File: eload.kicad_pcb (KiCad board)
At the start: 2 copper layers, 78.7 x 99.1 mm, 34 parts, among them J1 Device Power, J2 Input, J3 Conn_01x16_Socket, J4 SWD Header, J5 Conn_01x14_Pin, Q1 TIP122, U1 LM1117DT-3.3, U2 STM32F103C8T6, U3 AD8629, U4 MCP4725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

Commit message: WIP
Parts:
- added F1: 1.5A, Resistor_THT:R_Axial_DIN0204_L3.6mm_D1.6mm_P7.62mm_Horizontal, F.Cu at (50.3, 64.9)
- J3: value Conn_01x16_Socket -> JST Header
- J5: value Conn_01x14_Pin -> ~
- U3: footprint Package_SO:SOP-8_3.76x4.96mm_P1.27mm -> Package_SO:JEITA_SOIC-8_3.9x4.9mm_P1.27mm
- moved TP7 136.6 mm to (40.0, 56.0)
- moved TP3 102.4 mm to (32.0, 79.2)
- moved TP4 101.0 mm to (37.3, 75.9)
- moved TP1 87.6 mm to (39.2, 91.5)
- moved TP2 86.0 mm to (42.5, 91.5)
- moved TP6 82.2 mm to (80.9, 60.2)
- moved TP5 73.1 mm to (82.2, 67.0)
- moved Y1 50.9 mm to (49.2, 85.5), turned to 180 degrees
- moved J4 50.1 mm to (20.8, 132.9), turned to 180 degrees
- moved C8 49.4 mm to (75.6, 75.4), turned to 180 degrees
- moved C3 45.2 mm to (51.8, 93.5), turned to 180 degrees
- moved R4 44.6 mm to (81.2, 70.2), turned to 180 degrees
- moved R2 43.6 mm to (69.5, 86.5)
- moved U2 43.6 mm to (59.3, 86.5)
- moved R1 43.6 mm to (68.5, 89.0)
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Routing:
- net VCC: track 0.00 -> 26.3 mm
- net /VCC_sense: track 0.00 -> 25.8 mm
- net +3.3V: track 0.00 -> 12.2 mm
- net /Vctrl: track 0.00 -> 11.4 mm
- net Net-(Q1-B): track 0.00 -> 10.8 mm
- net /Vin: track 0.00 -> 8.61 mm
- net +5V: track 0.00 -> 8.39 mm
- net GND: track 0.00 -> 6.39 mm
- net Net-(U4-VOUT): track 0.00 -> 2.62 mm
- net /Vsense: track 0.00 -> 2.30 mm

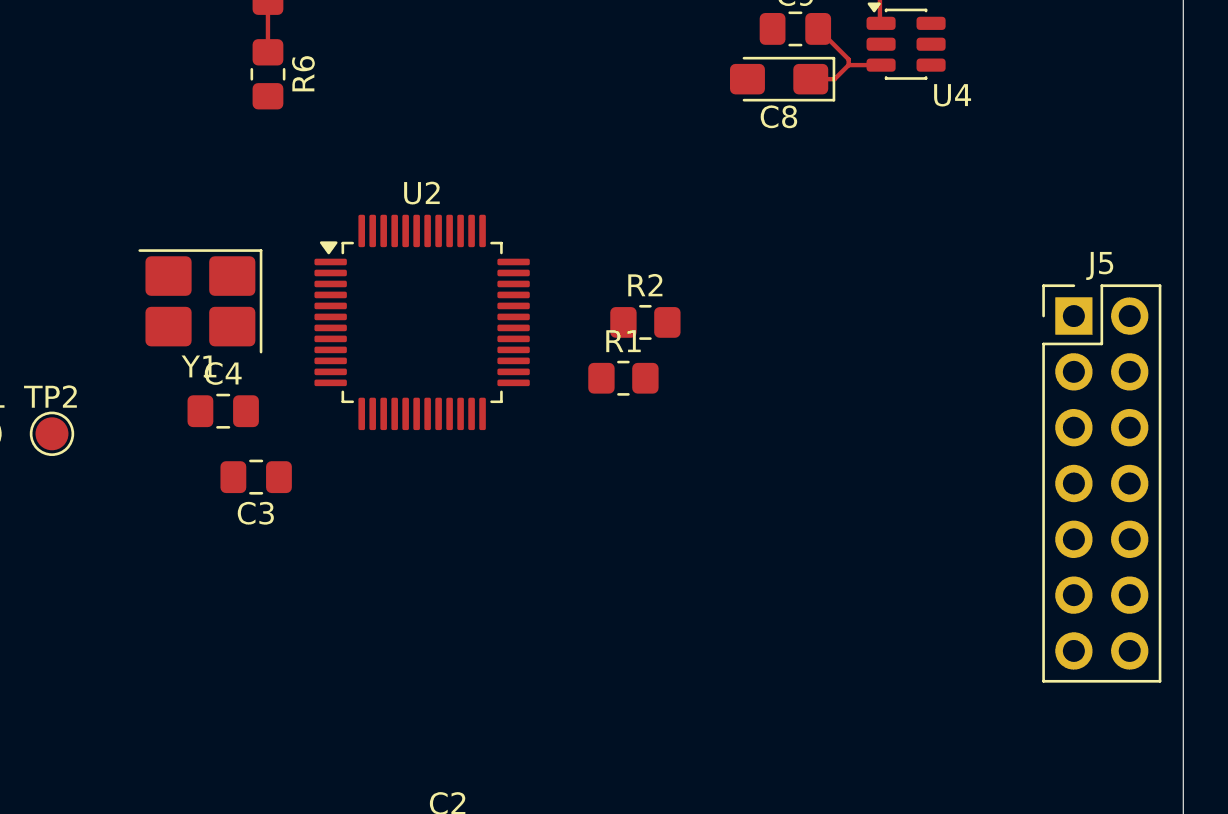
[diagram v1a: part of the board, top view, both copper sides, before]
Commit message: Routing power plane for STM32
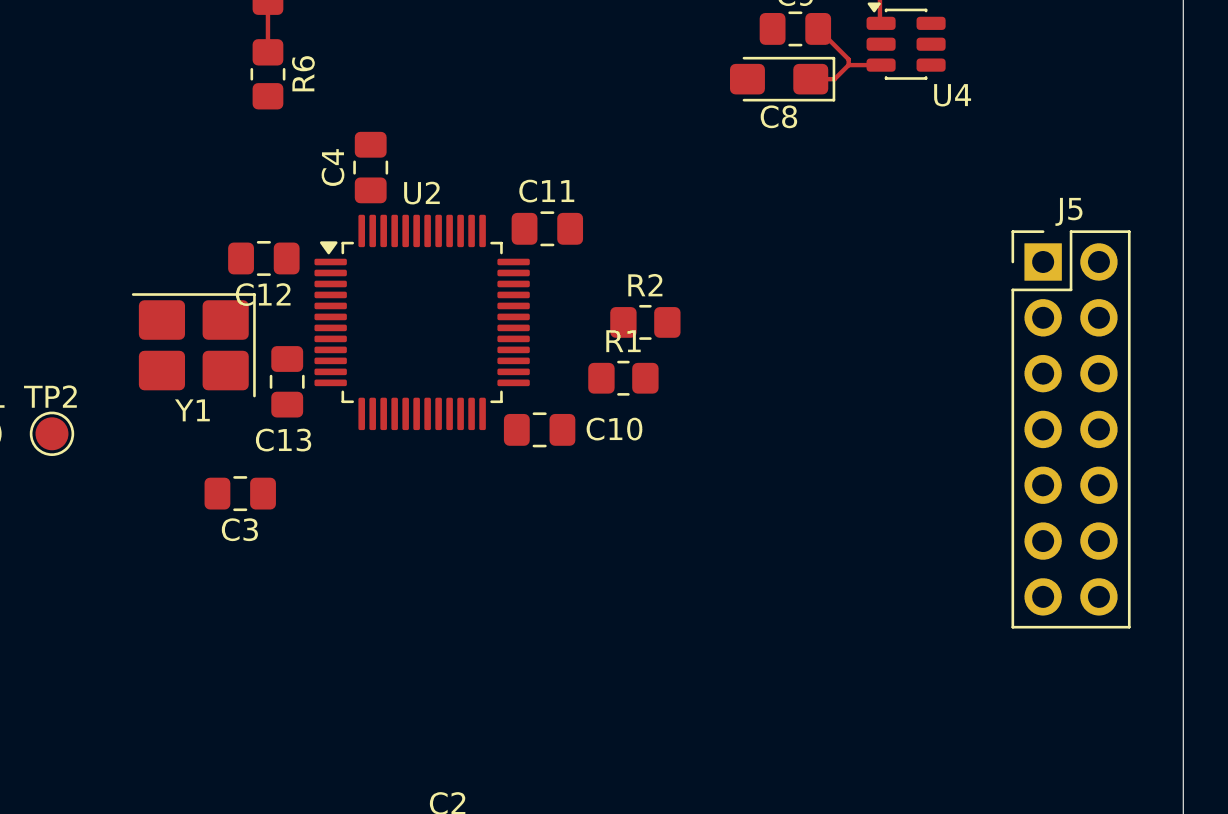
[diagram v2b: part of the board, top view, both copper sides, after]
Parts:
- added C10: 100nF, Capacitor_SMD:C_0805_2012Metric_Pad1.18x1.45mm_HandSolder, F.Cu at (64.7, 91.3)
- added C11: 100nF, Capacitor_SMD:C_0805_2012Metric_Pad1.18x1.45mm_HandSolder, F.Cu at (65.0, 82.2)
- added C12: 100nF, Capacitor_SMD:C_0805_2012Metric_Pad1.18x1.45mm_HandSolder, F.Cu at (52.1, 83.5)
- added C13: 100nF, Capacitor_SMD:C_0805_2012Metric_Pad1.18x1.45mm_HandSolder, F.Cu at (53.2, 89.2)
- R4: value 90K -> 89.8K
- U2: value STM32F103C8T6 -> STM32F103CBT6
- moved C4 13.0 mm to (57.0, 79.4), turned to 90 degrees
- moved J5 2.83 mm to (87.6, 83.7)
- moved Y1 2.02 mm to (49.0, 87.5)
- moved C3 1.04 mm to (51.1, 94.2)
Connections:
- C7 pad 1: +3.3V -> +5V
- J5 pad 11: /PB12 -> /PB14
- J5 pad 12: /PB13 -> /PB15
- J5 pad 13: /PB14 -> /PB12
- J5 pad 14: /PB15 -> /PB13
- J5 pad 2: /PA12 -> /PB6
- J5 pad 9: /PB6 -> /PA12
- U3 pad 8: +3.3V -> +5V
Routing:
- net +5V: track 8.39 -> 10.5 mm
- net +3.3V: track 12.2 -> 10.1 mm

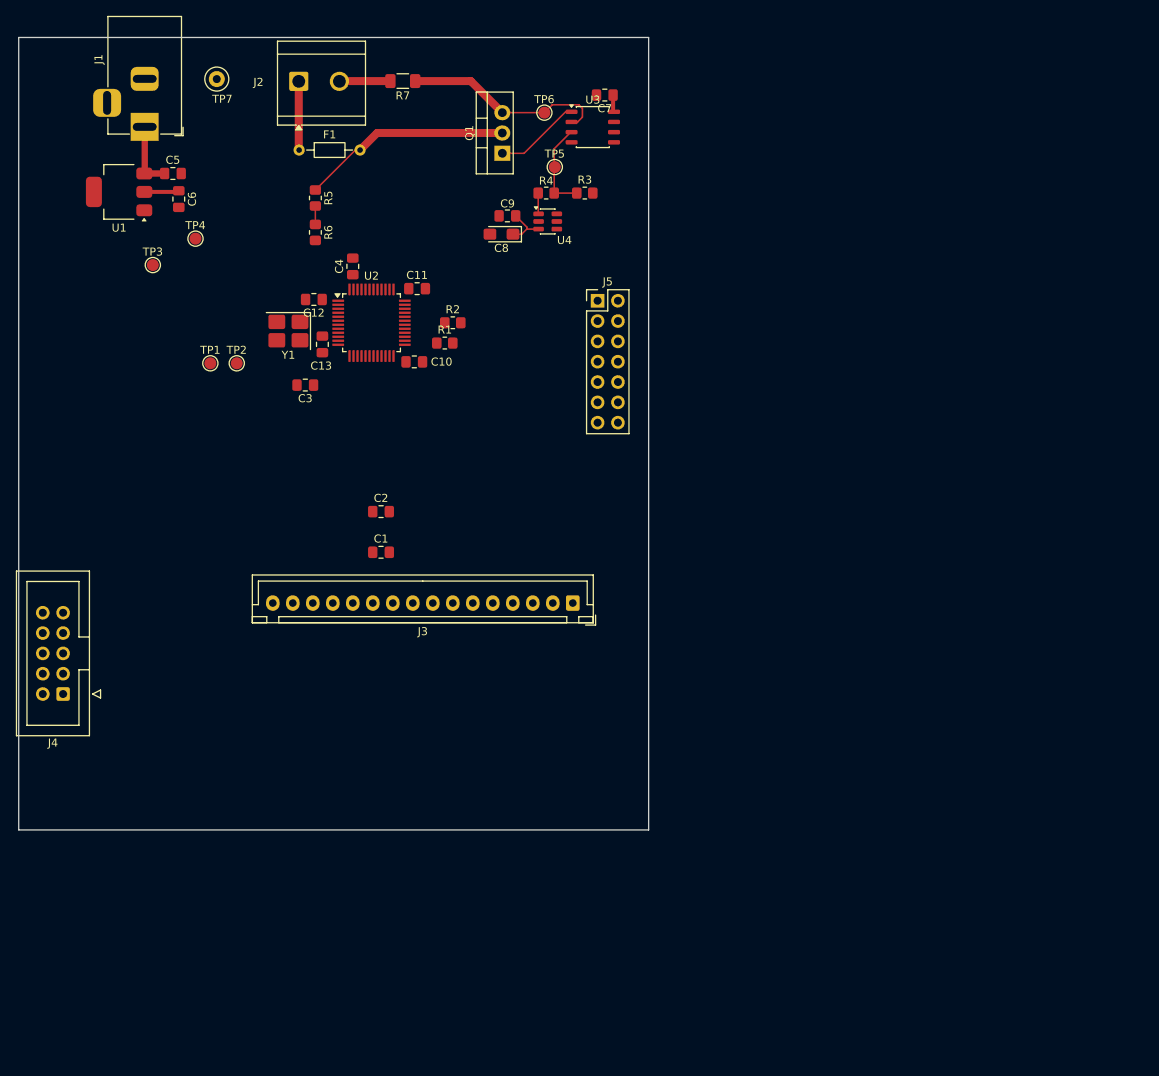
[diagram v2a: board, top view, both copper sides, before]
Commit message: 3D models added, mounting holes added
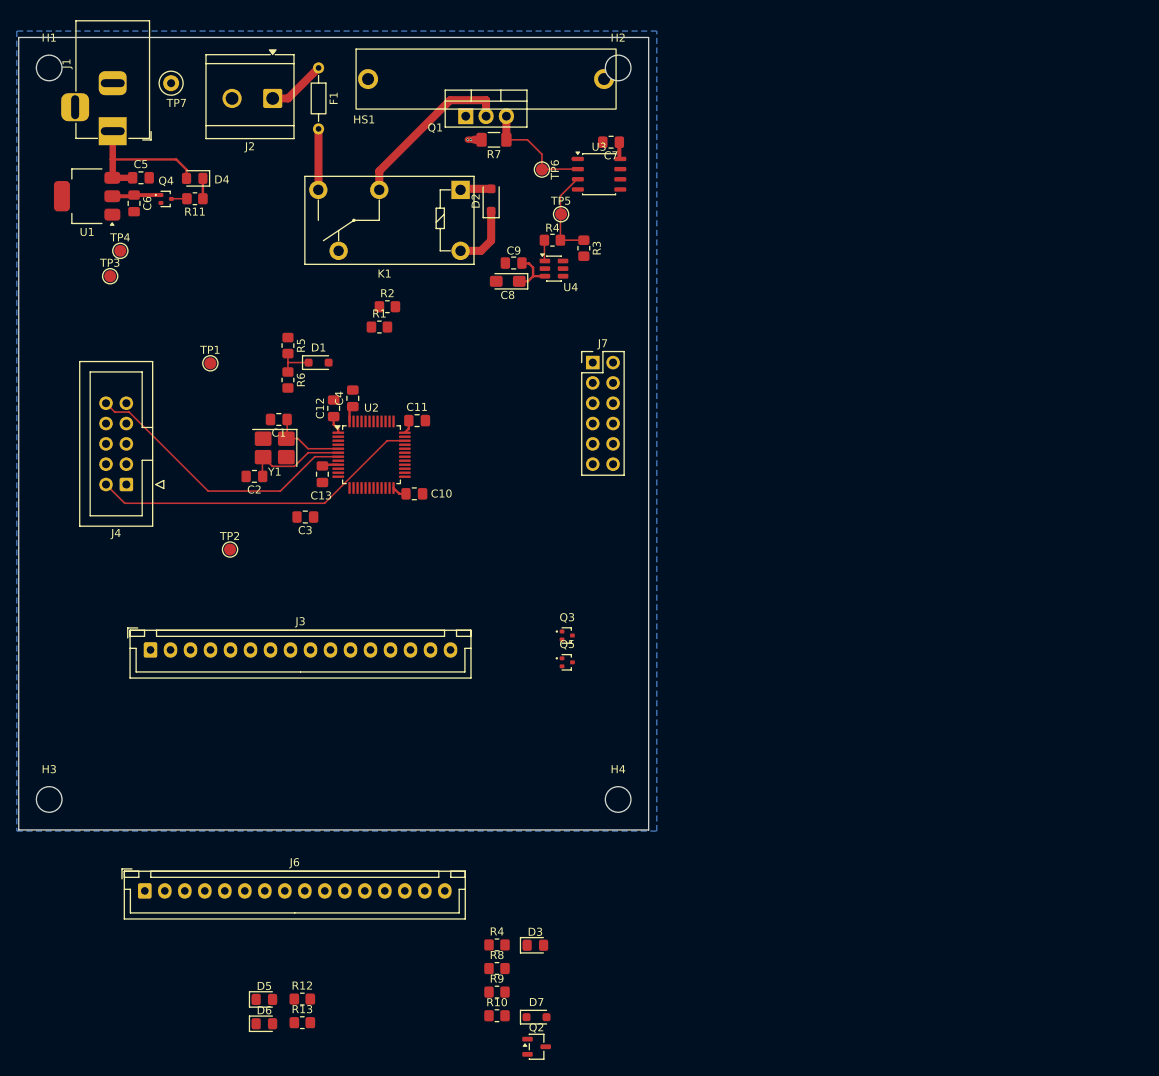
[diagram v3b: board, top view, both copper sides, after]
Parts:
- removed J5: ~, Connector_PinHeader_2.54mm:PinHeader_2x07_P2.54mm_Vertical
- added D1: BZT52C3V3S, Diode_SMD:D_SOD-323_HandSoldering, F.Cu at (52.7, 91.4)
- added D2: MBR120VLSFT1G, Diode_SMD:D_SOD-123F, F.Cu at (74.3, 71.1)
- added D3: 17-215/GHC-YR1S2/4T, LED_SMD:LED_0805_2012Metric_Pad1.15x1.40mm_HandSolder, F.Cu at (79.8, 164.3)
- added D4: 17-215/GHC-YR1S2/4T, LED_SMD:LED_0805_2012Metric_Pad1.15x1.40mm_HandSolder, F.Cu at (37.2, 68.4)
- added D5: 17-215/GHC-YR1S2/4T, LED_SMD:LED_0805_2012Metric_Pad1.15x1.40mm_HandSolder, F.Cu at (45.9, 171.0)
- added D6: 17-215/GHC-YR1S2/4T, LED_SMD:LED_0805_2012Metric_Pad1.15x1.40mm_HandSolder, F.Cu at (45.9, 174.1)
- added D7: BZT52C3V3S, Diode_SMD:D_SOD-323_HandSoldering, F.Cu at (80.0, 173.3)
- added H1: MountingHole, MountingHole:MountingHole_3.2mm_M3_DIN965, F.Cu at (19.1, 54.6)
- added H2: MountingHole, MountingHole:MountingHole_3.2mm_M3_DIN965, F.Cu at (90.2, 54.6)
- added H3: MountingHole, MountingHole:MountingHole_3.2mm_M3_DIN965, F.Cu at (19.1, 146.1)
- added H4: MountingHole, MountingHole:MountingHole_3.2mm_M3_DIN965, F.Cu at (90.2, 146.1)
- added HS1: Heatsink, eload:XSD1226-362, F.Cu at (73.7, 56.0)
- added J6: JST Header, Connector_JST:JST_XH_B16B-XH-A_1x16_P2.50mm_Vertical, F.Cu at (31.0, 157.5)
- added J7: Conn_02x06_Odd_Even, Connector_PinHeader_2.54mm:PinHeader_2x06_P2.54mm_Vertical, F.Cu at (87.0, 91.4)
- added K1: G5Q-1, Relay_THT:Relay_SPDT_Omron-G5Q-1, F.Cu at (70.5, 69.8)
- added Q2: HL 40N05, Package_TO_SOT_SMD:SOT-23-3, F.Cu at (80.0, 177.0)
- added Q3: DTC043Z, Package_TO_SOT_SMD:SOT-416, F.Cu at (83.8, 125.6)
- added Q4: DTC043Z, Package_TO_SOT_SMD:SOT-416, F.Cu at (33.7, 71.0)
- added Q5: DTC043Z, Package_TO_SOT_SMD:SOT-416, F.Cu at (83.8, 128.9)
- added R10: 150R, Resistor_SMD:R_0805_2012Metric_Pad1.20x1.40mm_HandSolder, F.Cu at (75.0, 173.1)
- added R11: 150R, Resistor_SMD:R_0805_2012Metric_Pad1.20x1.40mm_HandSolder, F.Cu at (37.3, 71.0)
- added R12: 220R, Resistor_SMD:R_0805_2012Metric_Pad1.20x1.40mm_HandSolder, F.Cu at (50.7, 171.0)
- added R13: 220R, Resistor_SMD:R_0805_2012Metric_Pad1.20x1.40mm_HandSolder, F.Cu at (50.7, 173.9)
- added R4: 10K, Resistor_SMD:R_0805_2012Metric_Pad1.20x1.40mm_HandSolder, F.Cu at (75.0, 164.2)
- added R8: 40K, Resistor_SMD:R_0805_2012Metric_Pad1.20x1.40mm_HandSolder, F.Cu at (75.0, 167.2)
- added R9: 40K, Resistor_SMD:R_0805_2012Metric_Pad1.20x1.40mm_HandSolder, F.Cu at (75.0, 170.1)
- moved J3 53.1 mm to (31.7, 127.4), turned to 0 degrees
- moved J4 27.4 mm to (28.7, 106.7)
- moved TP2 23.3 mm to (41.7, 114.8)
- moved C1 20.9 mm to (47.8, 98.6), turned to 180 degrees
- moved R5 18.8 mm to (48.9, 89.3)
- moved R6 18.8 mm to (48.9, 93.6)
- moved C10 16.5 mm to (64.7, 107.8)
- moved C11 16.5 mm to (65.0, 98.7)
- moved C3 16.5 mm to (51.1, 110.7)
- moved C4 16.5 mm to (57.0, 95.9)
- moved U2 16.5 mm to (59.3, 103.0)
- moved C2 16.4 mm to (44.7, 105.7), turned to 180 degrees
- moved C13 16.2 mm to (53.2, 105.4)
- moved Y1 14.7 mm to (47.2, 102.1)
- moved C12 13.8 mm to (54.6, 97.2), turned to 90 degrees
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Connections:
- F1 pad 2: VCC -> /Vfuse
- J3 pad 10: /D5 -> /D0
- J3 pad 11: /D4 -> /D1
- J3 pad 12: /D3 -> /D2
- J3 pad 13: /D2 -> /D3
- J3 pad 14: /D1 -> /D4
- J3 pad 15: /D0 -> /D5
- J3 pad 16: +3.3V -> /D6
- J3 pad 6: /RS -> /OvDetect
- J3 pad 7: /E -> /LoadEn
- J3 pad 8: /D7 -> /RS
- J3 pad 9: /D6 -> /E
- U2 pad 20: /BOOT1 -> unconnected-(U2-PB2-Pad20)
- U2 pad 31: /PA10 -> /LoadEn
- U2 pad 32: /PA11 -> /OvDetect
- U2 pad 38: /JTDI -> unconnected-(U2-PA15-Pad38)
- U2 pad 39: /JTDO -> unconnected-(U2-PB3-Pad39)
- U2 pad 40: /JNTRST -> unconnected-(U2-PB4-Pad40)
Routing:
- net /SWDIO: track 0.00 -> 41.6 mm
- net /~{RESET}: track 0.00 -> 35.4 mm
- net +5V: track 10.5 -> 29.4 mm
- net /OSC2: track 0.00 -> 13.0 mm
- net +3.3V: track 10.1 -> 22.2 mm
- net /VCC_sense: track 25.8 -> 14.6 mm
- net Net-(Q1-B): track 10.8 -> 0.75 mm
- net /OSC1: track 0.00 -> 9.46 mm
- net /Vfuse: track 0.00 -> 7.63 mm
- net GND: track 6.39 -> 0.74 mm, vias 0 -> 2
- net VCC: track 26.3 -> 21.4 mm
- net Net-(D2-A): track 0.00 -> 3.88 mm
- net /Vsense: track 2.30 -> 4.88 mm
- net Net-(D4-K): track 0.00 -> 2.54 mm
- net Net-(Q4-PadC): track 0.00 -> 1.96 mm
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- added copper zone on B.Cu, net GND

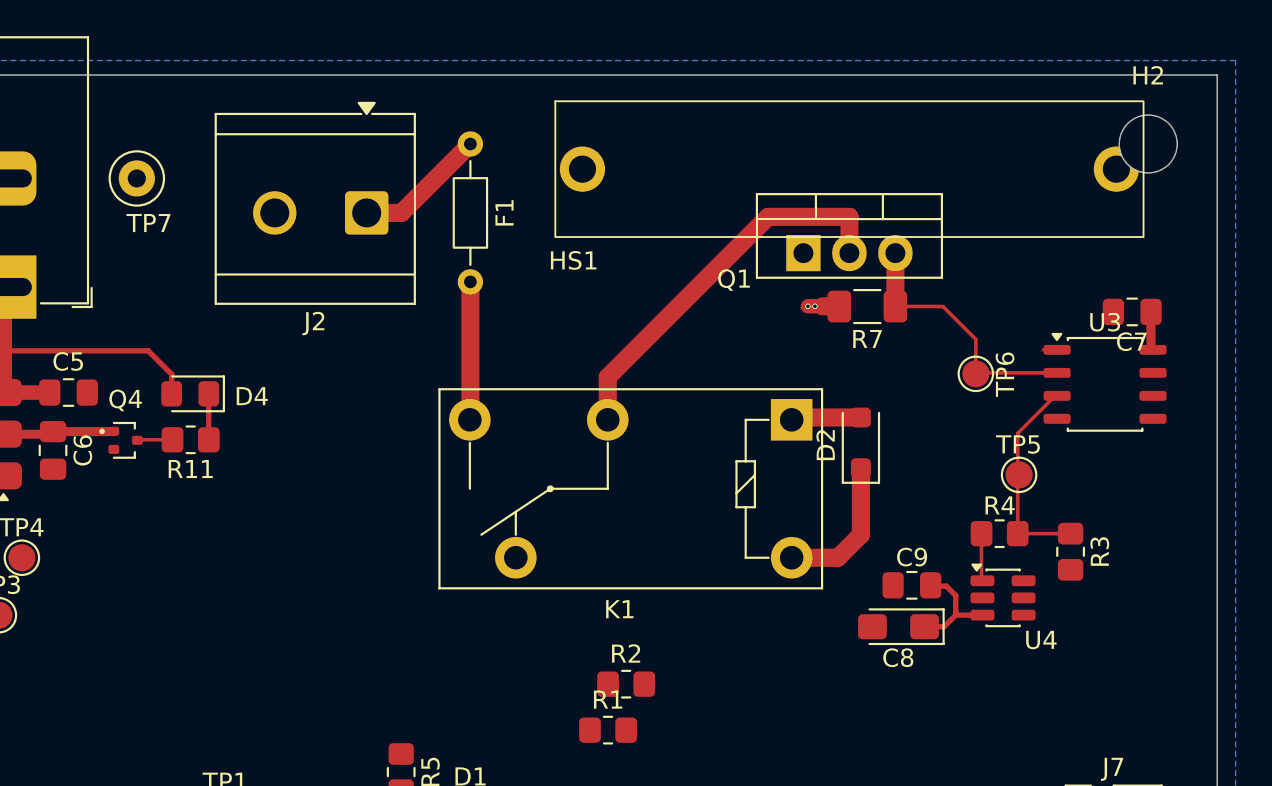
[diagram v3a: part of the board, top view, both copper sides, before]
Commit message: Update heatsink model
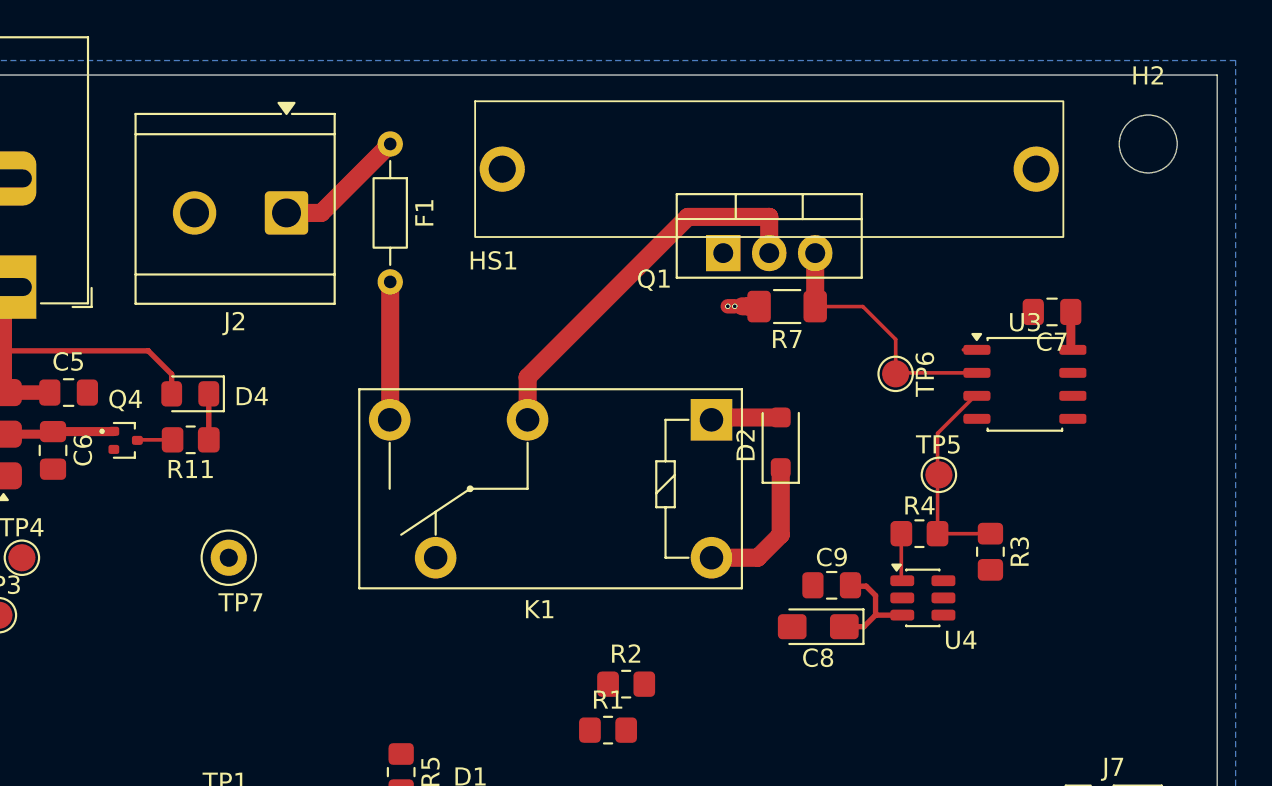
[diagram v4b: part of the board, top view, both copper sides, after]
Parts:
- moved TP7 21.6 mm to (39.4, 77.5)
- moved C8 4.43 mm to (71.9, 81.3)
- moved C9 4.43 mm to (72.7, 79.0)
- moved D2 4.43 mm to (69.9, 71.1)
- moved Q1 4.43 mm to (66.7, 60.6)
- moved R4 4.43 mm to (77.5, 76.1)
- moved R7 4.43 mm to (70.2, 63.6)
- moved F1 4.43 mm to (48.3, 54.6)
- moved J2 4.43 mm to (42.6, 58.4)
- moved C7 4.43 mm to (84.9, 63.9)
- moved HS1 4.43 mm to (69.2, 56.0)
- moved K1 4.43 mm to (66.0, 69.8)
- moved R3 4.43 mm to (81.5, 77.1)
- moved TP5 4.43 mm to (78.6, 72.9)
- moved TP6 4.43 mm to (76.2, 67.3)
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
